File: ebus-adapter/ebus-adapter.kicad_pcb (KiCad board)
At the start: 2 copper layers, 45.7 x 40.6 mm, 29 parts, among them J1 EBus-Connector, J2 Serial, Q1 BC337, U1 L7805, U2 LM393N, U3 4N25, U4 4N25

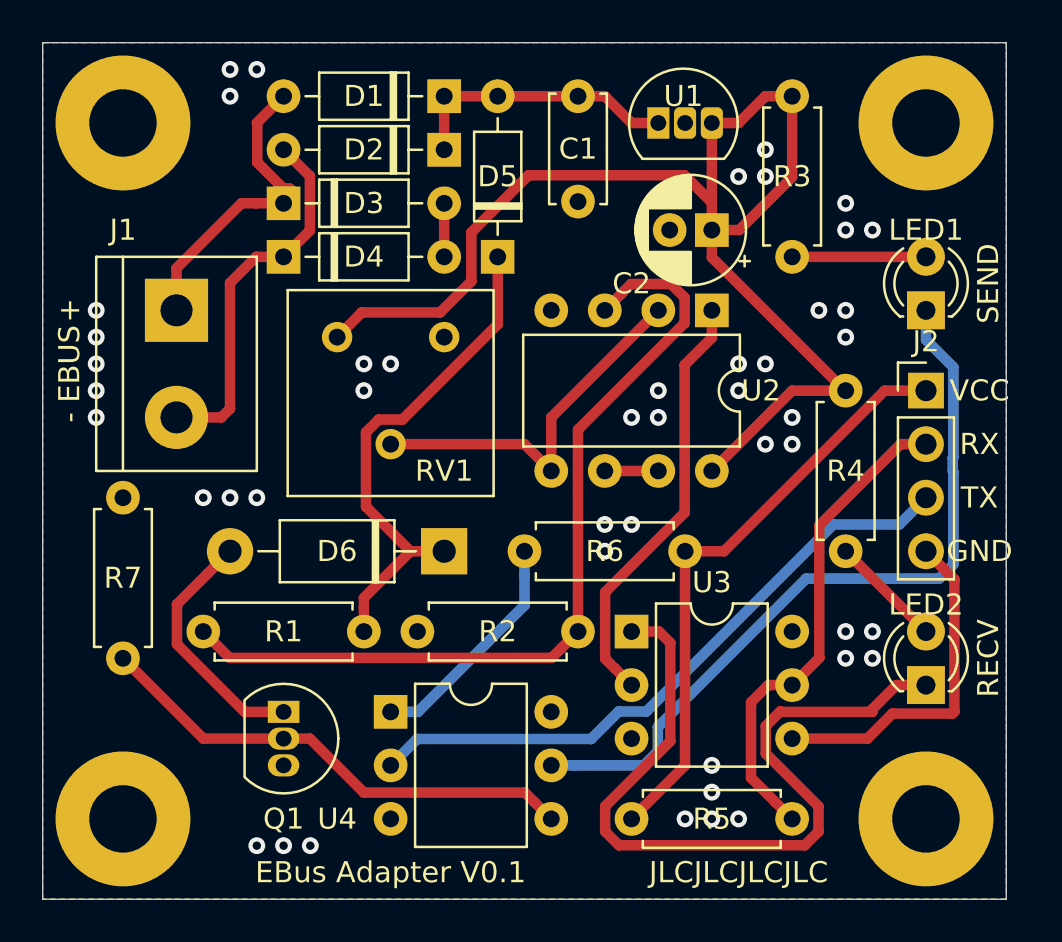
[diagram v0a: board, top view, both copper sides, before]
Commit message: Corrected footprint of 7805 voltage ragulator
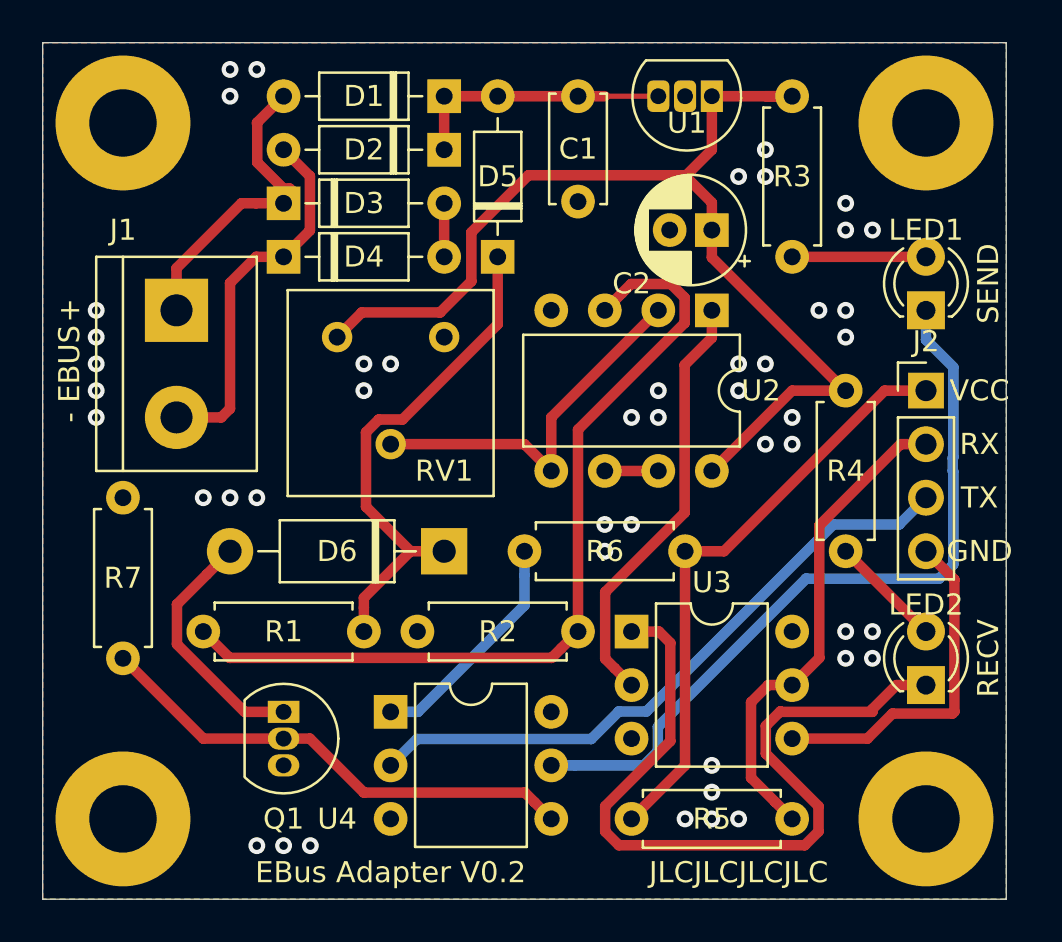
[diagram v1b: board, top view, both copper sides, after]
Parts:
- R1: value 20k -> 22k
- R2: value 5k -> 4.7k
- R6: value 130 -> 120
- U1: value L7805 -> L78L05
- moved U1 2.84 mm to (62.2, 94.0), turned to 180 degrees
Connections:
- U1 pad 1: Net-(C1-Pad1) -> +5V
- U1 pad 3: +5V -> Net-(C1-Pad1)
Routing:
- net +5V: track 59.2 -> 51.8 mm
- net Net-(C1-Pad1): track 13.2 -> 12.7 mm
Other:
- board text added: "EBus Adapter V0.2"
- board text removed: "EBus Adapter V0.1"
